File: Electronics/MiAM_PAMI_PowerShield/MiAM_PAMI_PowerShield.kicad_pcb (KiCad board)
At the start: 2 copper layers, 28.7 x 54.7 mm, 8 parts, among them U2 3V3, U3 MT3608, U4 LM7805_TO220, U5 ESP32-DEVKIT-V1

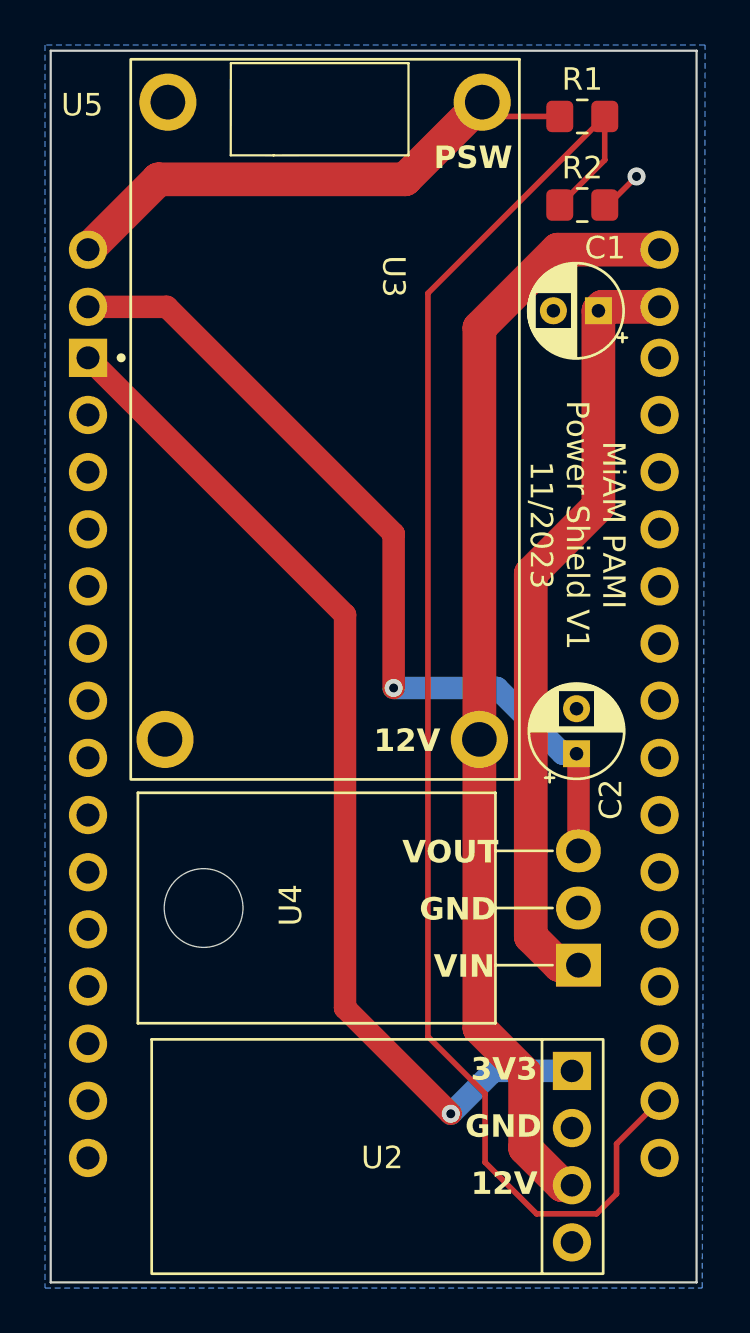
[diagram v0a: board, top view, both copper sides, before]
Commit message: Fix MT3608 footprint
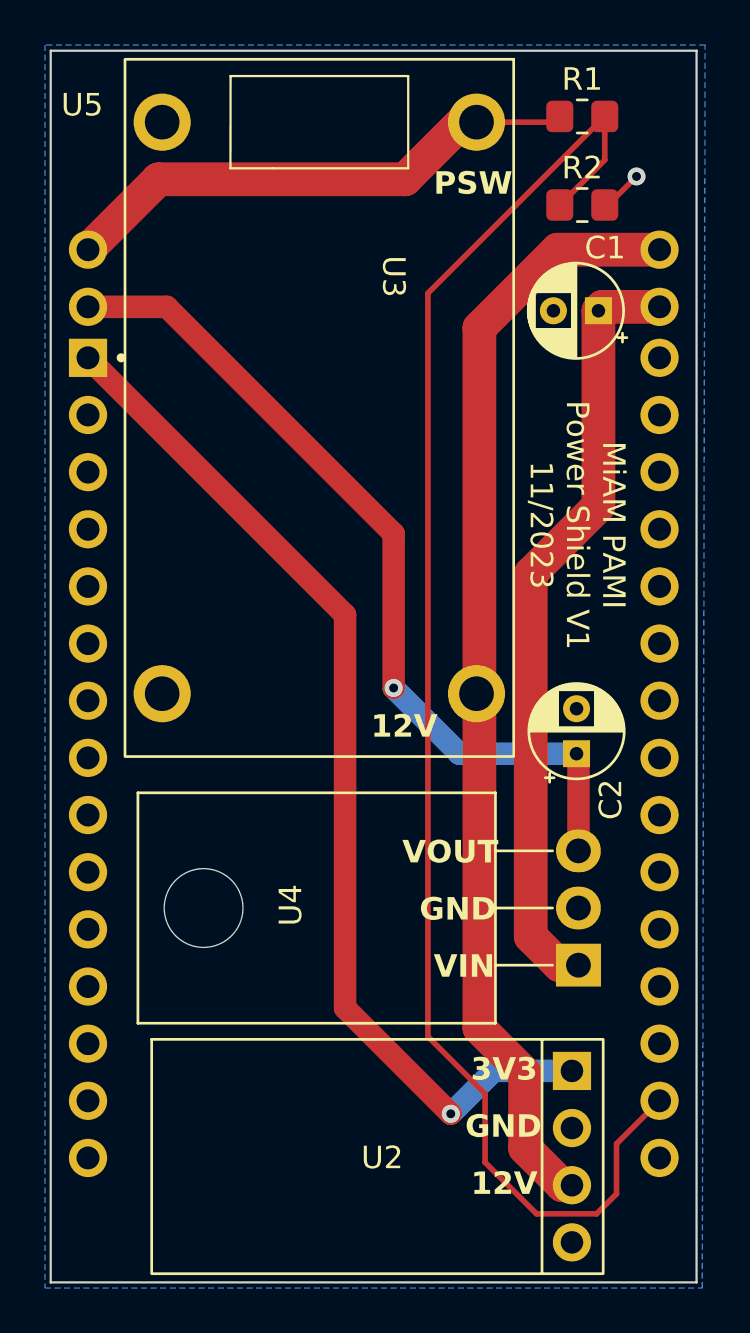
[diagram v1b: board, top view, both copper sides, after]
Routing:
- net /POWER_SWITCH: track 23.9 -> 23.4 mm
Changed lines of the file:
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@@
+        (effects (font (size 1 1) (thickness 0.15)))
+    )
+    (fp_text user "${REFERENCE}" (at 8.9154 0.0508 90) (layer "F.Fab")
         (effects (font (size 1 1) (thickness 0.15)))
     )
     (fp_text user "${REFERENCE}" (at 8.8554 2.6478 unlocked) (layer "F.Fab")
-        (effects (font (size 1 1) (thickness 0.15)))
-    )
-    (fp_text user "${REFERENCE}" (at 8.9154 0.0508 90) (layer "F.Fab")
         (effects (font (size 1 1) (thickness 0.15)))
     )
@@
         (effects (font (size 1 1) (thickness 0.15)))
     )
-    (fp_line (start -15.324 -3.9624) (end -15.324 3.932)
+    (fp_line (start -14.7486 -3.9497) (end -14.7486 3.9447)
       (stroke (width 0.1) (type solid)) (layer "F.SilkS"))
-    (fp_line (start -15.324 3.932) (end -11.2268 3.937)
+    (fp_line (start -14.7486 3.9447) (end -10.6514 3.9497)
       (stroke (width 0.1) (type solid)) (layer "F.SilkS"))
-    (fp_line (start -11.2268 -3.9624) (end -15.324 -3.9624)
+    (fp_line (start -10.6514 -3.9497) (end -14.7486 -3.9497)
       (stroke (width 0.1) (type solid)) (layer "F.SilkS"))
-    (fp_line (start -11.224 2.032) (end -11.2268 -3.9624)
+    (fp_line (start -10.6486 2.0447) (end -10.6514 -3.9497)
       (stroke (width 0.1) (type solid)) (layer "F.SilkS"))
-    (fp_line (start -11.224 2.032) (end -11.2268 3.937)
+    (fp_line (start -10.6486 2.0447) (end -10.6514 3.9497)
       (stroke (width 0.1) (type solid)) (layer "F.SilkS"))
-    (fp_rect (start -15.494 -8.89) (end 16.51 8.382)
+    (fp_rect (start -15.494 -8.636) (end 15.494 8.636)
       (stroke (width 0.12) (type solid)) (fill none) (layer "F.SilkS"))
-    (fp_line (start -15.724 -9.017) (end 16.637 -9.017)
-      (stroke (width 0.05) (type solid)) (layer "F.CrtYd"))
-    (fp_line (start -15.724 8.636) (end -15.724 -9.017)
-      (stroke (width 0.05) (type solid)) (layer "F.CrtYd"))
-    (fp_line (start 16.637 -9.017) (end 16.637 8.636)
-      (stroke (width 0.05) (type solid)) (layer "F.CrtYd"))
-    (fp_line (start 16.637 8.636) (end -15.724 8.636)
-      (stroke (width 0.05) (type solid)) (layer "F.CrtYd"))
-    (pad "1" thru_hole circle (at -13.589 -7.239 270) (size 2.54 2.54) (drill 1.54) (layers "*.Cu" "*.Mask")
+    (fp_rect (start -15.621 -8.763) (end 15.621 8.763)
+      (stroke (width 0.1) (type default)) (fill none) (layer "F.CrtYd"))
+    (fp_line (start -12.7 -6.985) (end -12.7 6.985)
+      (stroke (width 0.1) (type default)) (layer "F.Fab"))
+    (fp_line (start -12.7 -6.985) (end 12.7 -6.985)
+      (stroke (width 0.12) (type default)) (layer "F.Fab"))
+    (fp_line (start -12.7 6.985) (end 12.7 6.985)
+      (stroke (width 0.1) (type default)) (layer "F.Fab"))
+    (fp_line (start 12.7 -6.985) (end 12.7 6.985)
+      (stroke (width 0.1) (type default)) (layer "F.Fab"))
+    (fp_rect (start -15.621 -8.763) (end 15.621 8.763)
+      (stroke (width 0.1) (type default)) (fill none) (layer "F.Fab"))
+    (pad "1" thru_hole circle (at -12.7 -6.985 270) (size 2.54 2.54) (drill 1.54) (layers "*.Cu" "*.Mask")
       (net 5 "/POWER_SWITCH") (pinfunction "VIN+") (pintype "power_in"))
-    (pad "2" thru_hole circle (at -13.589 6.731 270) (size 2.54 2.54) (drill 1.54) (layers "*.Cu" "*.Mask")
+    (pad "2" thru_hole circle (at -12.7 6.985 270) (size 2.54 2.54) (drill 1.54) (layers "*.Cu" "*.Mask")
       (net 1 "GND") (pinfunction "VIN-") (pintype "passive"))
-    (pad "3" thru_hole circle (at 14.732 -7.112 270) (size 2.54 2.54) (drill 1.54) (layers "*.Cu" "*.Mask")
+    (pad "3" thru_hole circle (at 12.7 -6.985 270) (size 2.54 2.54) (drill 1.54) (layers "*.Cu" "*.Mask")
       (net 2 "+12V") (pinfunction "OUT+") (pintype "power_out"))
-    (pad "4" thru_hole circle (at 14.732 6.858 270) (size 2.54 2.54) (drill 1.54) (layers "*.Cu" "*.Mask")
+    (pad "4" thru_hole circle (at 12.7 6.985 270) (size 2.54 2.54) (drill 1.54) (layers "*.Cu" "*.Mask")
       (net 1 "GND") (pinfunction "OUT-") (pintype "passive"))
+    (group "" (id 83b4b077-56a0-4da5-bcb2-af6122c579b9)
+      (members
+        716e071e-85a7-453c-8c99-e3af56eeea61
+        790ea8cb-c838-473f-91a7-b03e39cf4e26
+        8edffcc2-abbf-4c4e-9e54-c33058f82b21
+        ab4800d1-e870-4948-a01b-73b8ca71de29
+        c0720cc9-41b0-473a-af28-fc31d5976b43
+      )
+    )
   )
   (footprint "Package_TO_SOT_THT:TO-220-3_Horizontal_TabDown" (layer "F.Cu")
@@
     (effects (font (size 1 1) (thickness 0.25) bold) (justify left bottom))
   )
-  (gr_text "PSW" (at 100.33 59.944) (layer "F.SilkS")
+  (gr_text "PSW" (at 100.33 61.087) (layer "F.SilkS")
     (effects (font (size 1 1) (thickness 0.25) bold) (justify left bottom))
   )
@@
     (effects (font (size 1 1) (thickness 0.25) bold) (justify left bottom))
   )
-  (gr_text "12V" (at 97.663 85.852) (layer "F.SilkS")
+  (gr_text "12V" (at 97.536 85.217) (layer "F.SilkS")
     (effects (font (size 1 1) (thickness 0.25) bold) (justify left bottom))
   )
@@
   (segment (start 105.8385 63.4525) (end 110.3695 63.4525) (width 1.5) (layer "F.Cu") (net 2))
   (segment (start 102.362 66.929) (end 105.8385 63.4525) (width 1.5) (layer "F.Cu") (net 2))
-  (segment (start 102.362 98.044) (end 102.362 85.217) (width 1.5) (layer "F.Cu") (net 2))
-  (segment (start 102.362 85.217) (end 102.362 66.929) (width 1.5) (layer "F.Cu") (net 2))
+  (segment (start 102.362 98.044) (end 102.362 66.929) (width 1.5) (layer "F.Cu") (net 2))
   (segment (start 104.902 106.299) (end 107.569 106.299) (width 0.25) (layer "F.Cu") (net 3))
   (segment (start 108.458 105.41) (end 108.458 103.189) (width 0.25) (layer "F.Cu") (net 3))
@@
   (segment (start 106.4768 99.949) (end 102.997 99.949) (width 1) (layer "B.Cu") (net 4))
   (segment (start 102.997 99.949) (end 101.092 101.854) (width 1) (layer "B.Cu") (net 4))
-  (segment (start 103.124 57.531) (end 102.489 56.896) (width 0.25) (layer "F.Cu") (net 5))
+  (segment (start 102.235 57.785) (end 105.68 57.785) (width 0.25) (layer "F.Cu") (net 5))
+  (segment (start 88.097 60.325) (end 84.9695 63.4525) (width 1.5) (layer "F.Cu") (net 5))
   (segment (start 99.06 60.325) (end 88.097 60.325) (width 1.5) (layer "F.Cu") (net 5))
-  (segment (start 105.934 57.531) (end 103.124 57.531) (width 0.25) (layer "F.Cu") (net 5))
-  (segment (start 102.489 56.896) (end 99.06 60.325) (width 1.5) (layer "F.Cu") (net 5))
-  (segment (start 88.097 60.325) (end 84.9695 63.4525) (width 1.5) (layer "F.Cu") (net 5))
+  (segment (start 102.235 57.785) (end 101.6 57.785) (width 1.5) (layer "F.Cu") (net 5))
+  (segment (start 105.68 57.785) (end 105.934 57.531) (width 0.25) (layer "F.Cu") (net 5))
+  (segment (start 101.6 57.785) (end 99.06 60.325) (width 1.5) (layer "F.Cu") (net 5))
   (segment (start 107.8271 65.9925) (end 110.3695 65.9925) (width 1.5) (layer "F.Cu") (net 6))
   (segment (start 107.6526 66.167) (end 107.8271 65.9925) (width 1.5) (layer "F.Cu") (net 6))
@@
   (segment (start 106.766 85.938) (end 106.68 85.852) (width 1) (layer "F.Cu") (net 7))
   (via (at 98.552 82.931) (size 0.8) (drill 0.4) (layers "F.Cu" "B.Cu") (net 7))
-  (segment (start 98.552 82.931) (end 103.1457 82.931) (width 1) (layer "B.Cu") (net 7))
-  (segment (start 106.0667 85.852) (end 106.68 85.852) (width 1) (layer "B.Cu") (net 7))
-  (segment (start 103.1457 82.931) (end 106.0667 85.852) (width 1) (layer "B.Cu") (net 7))
+  (segment (start 101.473 85.852) (end 106.68 85.852) (width 1) (layer "B.Cu") (net 7))
+  (segment (start 98.552 82.931) (end 101.473 85.852) (width 1) (layer "B.Cu") (net 7))
   (zone (net 1) (net_name "GND") (layer "B.Cu") (hatch edge 0.5)
     (connect_pads (clearance 0.508))

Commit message: Fix shield footprint
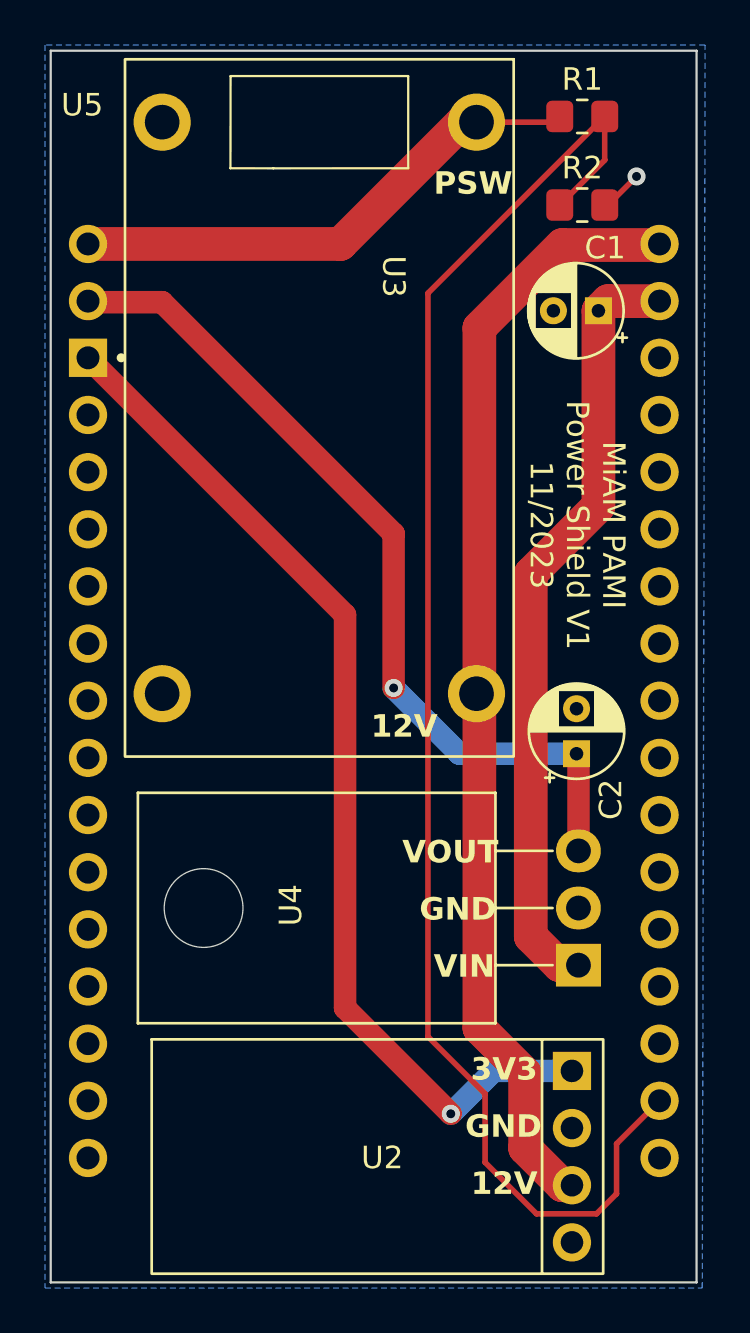
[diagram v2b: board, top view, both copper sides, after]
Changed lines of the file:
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@@
+        (effects (font (size 1 1) (thickness 0.15)))
+    )
+    (fp_text user "${REFERENCE}" (at 8.8554 2.6478 unlocked) (layer "F.Fab")
         (effects (font (size 1 1) (thickness 0.15)))
     )
     (fp_text user "${REFERENCE}" (at 8.9154 0.0508 90) (layer "F.Fab")
-        (effects (font (size 1 1) (thickness 0.15)))
-    )
-    (fp_text user "${REFERENCE}" (at 8.8554 2.6478 unlocked) (layer "F.Fab")
         (effects (font (size 1 1) (thickness 0.15)))
     )
@@
     (pad "4" thru_hole circle (at 12.7 6.985 270) (size 2.54 2.54) (drill 1.54) (layers "*.Cu" "*.Mask")
       (net 1 "GND") (pinfunction "OUT-") (pintype "passive"))
-    (group "" (id 83b4b077-56a0-4da5-bcb2-af6122c579b9)
+    (group "" (id cc9539fe-504e-45b9-947c-96e3c7fd985b)
       (members
-        716e071e-85a7-453c-8c99-e3af56eeea61
-        790ea8cb-c838-473f-91a7-b03e39cf4e26
-        8edffcc2-abbf-4c4e-9e54-c33058f82b21
-        ab4800d1-e870-4948-a01b-73b8ca71de29
-        c0720cc9-41b0-473a-af28-fc31d5976b43
+        19dc727e-1860-44d8-a8b4-629d52e1a297
+        40a31ed4-2193-4e48-a3ee-cb120146807f
+        45f467f5-2af5-48ce-9133-8145cff8240f
+        6040cf2f-212e-45fd-b588-42303bf58670
+        ad8fbdd5-e5b5-4570-a929-00433c570138
       )
     )
@@
     (fp_line (start -14.28 -25.475) (end -3.211 -25.475)
       (stroke (width 0.127) (type solid)) (layer "F.Fab"))
-    (fp_line (start -14.28 25.475) (end -14.28 -25.475)
+    (fp_line (start -14.28 25.221) (end -14.28 -25.475)
       (stroke (width 0.127) (type solid)) (layer "F.Fab"))
     (fp_line (start -14.28 25.475) (end -8.91 25.475)
@@
     (pad "30" thru_hole circle (at 12.7 -15.515) (size 1.7 1.7) (drill 1.02) (layers "*.Cu" "*.Mask")
       (net 34 "unconnected-(U5-VIN-Pad30)") (pinfunction "VIN") (pintype "input+no_connect"))
-    (pad "SH1" thru_hole circle (at 12.7 -17.78) (size 1.7 1.7) (drill 1.02) (layers "*.Cu" "*.Mask")
+    (pad "SH1" thru_hole circle (at 12.7 -18.034) (size 1.7 1.7) (drill 1.02) (layers "*.Cu" "*.Mask")
       (net 6 "/EMERGENCY_BUTTON") (pinfunction "EMG_BUT") (pintype "passive"))
-    (pad "SH2" thru_hole circle (at 12.7 -20.32) (size 1.7 1.7) (drill 1.02) (layers "*.Cu" "*.Mask")
+    (pad "SH2" thru_hole circle (at 12.7 -20.574) (size 1.7 1.7) (drill 1.02) (layers "*.Cu" "*.Mask")
       (net 2 "+12V") (pinfunction "12V") (pintype "passive"))
-    (pad "SH3" thru_hole circle (at -12.7 -17.78) (size 1.7 1.7) (drill 1.02) (layers "*.Cu" "*.Mask")
+    (pad "SH3" thru_hole circle (at -12.7 -18.034) (size 1.7 1.7) (drill 1.02) (layers "*.Cu" "*.Mask")
       (net 7 "/5V_POWER") (pinfunction "SERVO_V") (pintype "passive"))
-    (pad "SH4" thru_hole circle (at -12.7 -20.32) (size 1.7 1.7) (drill 1.02) (layers "*.Cu" "*.Mask")
+    (pad "SH4" thru_hole circle (at -12.7 -20.574) (size 1.7 1.7) (drill 1.02) (layers "*.Cu" "*.Mask")
       (net 5 "/POWER_SWITCH") (pinfunction "POW_SW") (pintype "passive"))
   )
@@
   (segment (start 107.934 61.468) (end 108.077 61.468) (width 0.25) (layer "F.Cu") (net 1))
   (via (at 109.347 60.198) (size 0.8) (drill 0.4) (layers "F.Cu" "B.Cu") (net 1))
+  (segment (start 102.362 98.044) (end 102.362 66.929) (width 1.5) (layer "F.Cu") (net 2))
+  (segment (start 102.362 66.929) (end 106.045 63.246) (width 1.5) (layer "F.Cu") (net 2))
+  (segment (start 106.4768 105.029) (end 106.045 105.029) (width 1.5) (layer "F.Cu") (net 2))
+  (segment (start 110.322 63.246) (end 110.3695 63.1985) (width 1.5) (layer "F.Cu") (net 2))
+  (segment (start 104.394 103.378) (end 104.394 100.076) (width 1.5) (layer "F.Cu") (net 2))
+  (segment (start 106.045 63.246) (end 110.322 63.246) (width 1.5) (layer "F.Cu") (net 2))
   (segment (start 104.394 100.076) (end 102.362 98.044) (width 1.5) (layer "F.Cu") (net 2))
-  (segment (start 104.394 103.378) (end 104.394 100.076) (width 1.5) (layer "F.Cu") (net 2))
-  (segment (start 106.4768 105.029) (end 106.045 105.029) (width 1.5) (layer "F.Cu") (net 2))
   (segment (start 106.045 105.029) (end 104.394 103.378) (width 1.5) (layer "F.Cu") (net 2))
-  (segment (start 105.8385 63.4525) (end 110.3695 63.4525) (width 1.5) (layer "F.Cu") (net 2))
-  (segment (start 102.362 66.929) (end 105.8385 63.4525) (width 1.5) (layer "F.Cu") (net 2))
-  (segment (start 102.362 98.044) (end 102.362 66.929) (width 1.5) (layer "F.Cu") (net 2))
   (segment (start 104.902 106.299) (end 107.569 106.299) (width 0.25) (layer "F.Cu") (net 3))
   (segment (start 108.458 105.41) (end 108.458 103.189) (width 0.25) (layer "F.Cu") (net 3))
@@
   (segment (start 102.997 99.949) (end 101.092 101.854) (width 1) (layer "B.Cu") (net 4))
   (segment (start 102.235 57.785) (end 105.68 57.785) (width 0.25) (layer "F.Cu") (net 5))
-  (segment (start 88.097 60.325) (end 84.9695 63.4525) (width 1.5) (layer "F.Cu") (net 5))
-  (segment (start 99.06 60.325) (end 88.097 60.325) (width 1.5) (layer "F.Cu") (net 5))
+  (segment (start 101.6 57.785) (end 96.1865 63.1985) (width 1.5) (layer "F.Cu") (net 5))
+  (segment (start 105.68 57.785) (end 105.934 57.531) (width 0.25) (layer "F.Cu") (net 5))
   (segment (start 102.235 57.785) (end 101.6 57.785) (width 1.5) (layer "F.Cu") (net 5))
-  (segment (start 105.68 57.785) (end 105.934 57.531) (width 0.25) (layer "F.Cu") (net 5))
-  (segment (start 101.6 57.785) (end 99.06 60.325) (width 1.5) (layer "F.Cu") (net 5))
-  (segment (start 107.8271 65.9925) (end 110.3695 65.9925) (width 1.5) (layer "F.Cu") (net 6))
-  (segment (start 107.6526 66.167) (end 107.8271 65.9925) (width 1.5) (layer "F.Cu") (net 6))
+  (segment (start 96.1865 63.1985) (end 84.9695 63.1985) (width 1.5) (layer "F.Cu") (net 5))
   (segment (start 104.648 77.851) (end 107.6526 74.8464) (width 1.5) (layer "F.Cu") (net 6))
   (segment (start 104.648 93.98) (end 104.648 77.851) (width 1.5) (layer "F.Cu") (net 6))
+  (segment (start 108.0811 65.7385) (end 110.3695 65.7385) (width 1.5) (layer "F.Cu") (net 6))
+  (segment (start 107.6526 66.167) (end 108.0811 65.7385) (width 1.5) (layer "F.Cu") (net 6))
   (segment (start 106.766 95.25) (end 105.918 95.25) (width 1.5) (layer "F.Cu") (net 6))
   (segment (start 105.918 95.25) (end 104.648 93.98) (width 1.5) (layer "F.Cu") (net 6))
   (segment (start 107.6526 74.8464) (end 107.6526 66.167) (width 1.5) (layer "F.Cu") (net 6))
+  (segment (start 84.9695 65.7385) (end 85.017 65.786) (width 1) (layer "F.Cu") (net 7))
   (segment (start 106.766 90.17) (end 106.766 85.938) (width 1) (layer "F.Cu") (net 7))
-  (segment (start 88.4715 65.9925) (end 98.552 76.073) (width 1) (layer "F.Cu") (net 7))
+  (segment (start 85.017 65.786) (end 88.265 65.786) (width 1) (layer "F.Cu") (net 7))
+  (segment (start 88.265 65.786) (end 98.552 76.073) (width 1) (layer "F.Cu") (net 7))
   (segment (start 98.552 76.073) (end 98.552 82.931) (width 1) (layer "F.Cu") (net 7))
-  (segment (start 84.9695 65.9925) (end 88.4715 65.9925) (width 1) (layer "F.Cu") (net 7))
   (segment (start 106.766 85.938) (end 106.68 85.852) (width 1) (layer "F.Cu") (net 7))
   (via (at 98.552 82.931) (size 0.8) (drill 0.4) (layers "F.Cu" "B.Cu") (net 7))
